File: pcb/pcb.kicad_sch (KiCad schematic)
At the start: 72 parts

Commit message: A  RP2040_Minimal.kicad_sym A  RP2040_minimal.pretty/8-USON-Handsolder.kicad_mod A  RP2040_minimal.pretty/8-USON.kicad_mod A  RP2040_minimal.pretty/C_0402_1005Metric.kicad_mod A  RP2040_minimal.pretty/C_0603_1608Metric.kicad_mod A  RP2040_minimal.pretty/C_0603_1608Metric_Pad1.08x0.95mm_HandSolder.kicad_mod A  RP2040_minimal.pretty/C_1206_3216Metric.kicad_mod A  RP2040_minimal.pretty/Crystal_SMD_2520-4Pin_2.5x2.0mm-Handsolder.kicad_mod A  RP2040_minimal.pretty/Crystal_SMD_HC49-US.kicad_mod A  RP2040_minimal.pretty/D_0402_1005Metric.kicad_mod A  RP2040_minimal.pretty/D_SOD-523.kicad_mod A  RP2040_minimal.pretty/Diodes_U_DFN1212_3.kicad_mod A  RP2040_minimal.pretty/Diodes_U_DFN1212_3_Handsolder.kicad_mod A  RP2040_minimal.pretty/LED_0402_1005Metric.kicad_mod A  RP2040_minimal.pretty/LED_Driver_Mod_Conn.kicad_mod A  RP2040_minimal.pretty/LED_Driver_Mod_Conn_1.27.kicad_mod A  RP2040_minimal.pretty/Module_Conn_Regular.kicad_mod A  RP2040_minimal.pretty/Module_Conn_Regular2.kicad_mod A  RP2040_minimal.pretty/Module_Conn_Regular_Outline.kicad_mod A  RP2040_minimal.pretty/QFN-28-1EP_4x4mm_P0.4mm_EP2.3x2.3mm-Handsolder.kicad_mod A  RP2040_minimal.pretty/QFN-28-1EP_4x4mm_P0.4mm_EP2.3x2.3mm.kicad_mod A  RP2040_minimal.pretty/RP2040-QFN-56-Handsolder.kicad_mod A  RP2040_minimal.pretty/RP2040-QFN-56.kicad_mod A  RP2040_minimal.pretty/R_0402_1005Metric.kicad_mod A  RP2040_minimal.pretty/R_0603_1608Metric_Pad0.98x0.95mm_HandSolder.kicad_mod A  RP2040_minimal.pretty/SW_CK_KXT3.kicad_mod A  RP2040_minimal.pretty/SW_SPST_Panasonic_EVPAF.kicad_mod A  RP2040_minimal.pretty/SW_Side_EVPAV.kicad_mod A  RP2040_minimal.pretty/SW_XKB_TS_2030.kicad_mod A  RP2040_minimal.pretty/USB_Micro-B_Amphenol_10103594-0001LF_Horizontal_modified.kicad_mod A  RP2040_minimal.pretty/XSON-8-1EP_4x4mm.kicad_mod M  border.py M  notes/notes.md M  pcb/fp-lib-table M  pcb/pcb.kicad_pcb M  pcb/pcb.kicad_prl M  pcb/pcb.kicad_sch M  plate/plate.kicad_pcb M  plate/plate.kicad_sch R  tmr-footprints/Switch_Cutout2_MX.kic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
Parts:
- S64, S66: footprint tmr-lib:sw_lowpro_combo_MDT -> tmr-lib:sw_lowpro_combo_2u_MDT
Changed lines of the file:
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@@
 			)
 		)
-		(property "Footprint" "tmr-lib:sw_lowpro_combo_MDT"
+		(property "Footprint" "tmr-lib:sw_lowpro_combo_2u_MDT"
 			(at 132.08 147.32 0)
 			(effects
@@
 			)
 		)
-		(property "Footprint" "tmr-lib:sw_lowpro_combo_MDT"
+		(property "Footprint" "tmr-lib:sw_lowpro_combo_2u_MDT"
 			(at 172.72 147.32 0)
 			(effects

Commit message: M  border.py A  notes/keyfrequency M  pcb/pcb.kicad_pcb M  pcb/pcb.kicad_prl M  pcb/pcb.kicad_sch M  place.py A  tmr-footprints/LED-6028.kicad_mod D  tmr-footprints/LED_1206_THT.kicad_mod M  tmr-footprints/sw_lowpro_combo_2u_MDT.kicad_mod A  tmr-footprints/sw_lowpro_combo_2u_MDT_L.kicad_mod A  tmr-footprints/sw_lowpro_combo_2u_MDT_R.kicad_mod M  tmr-footprints/sw_lowpro_combo_MDT.kicad_mod M  tmr-footprints/sw_lowpro_combo_MDT_led.kicad_mod
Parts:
- S64: footprint tmr-lib:sw_lowpro_combo_2u_MDT -> tmr-lib:sw_lowpro_combo_2u_MDT_L
- S66: footprint tmr-lib:sw_lowpro_combo_2u_MDT -> tmr-lib:sw_lowpro_combo_2u_MDT_R
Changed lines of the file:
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@@
 			)
 		)
-		(property "Footprint" "tmr-lib:sw_lowpro_combo_2u_MDT"
+		(property "Footprint" "tmr-lib:sw_lowpro_combo_2u_MDT_L"
 			(at 132.08 147.32 0)
 			(effects
@@
 			)
 		)
-		(property "Footprint" "tmr-lib:sw_lowpro_combo_2u_MDT"
+		(property "Footprint" "tmr-lib:sw_lowpro_combo_2u_MDT_R"
 			(at 172.72 147.32 0)
 			(effects

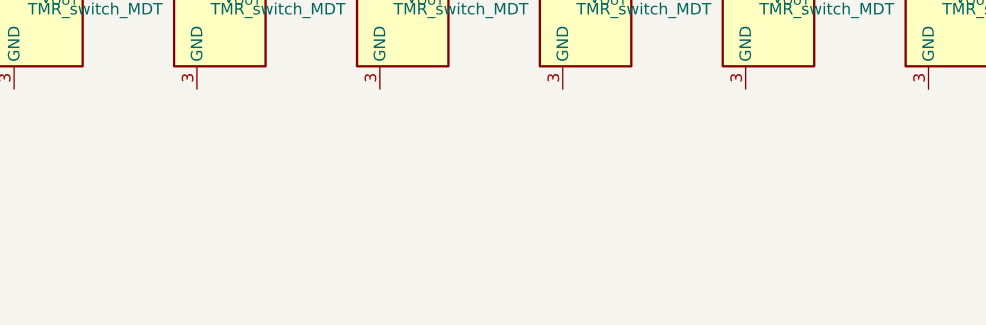
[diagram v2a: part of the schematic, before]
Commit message: M  notes/components.md M  pcb/pcb.kicad_pcb M  pcb/pcb.kicad_sch M  place.py D  tmr-footprints/sw_lowpro_combo_2u_MDT.kicad_mod D  tmr-footprints/sw_lowpro_combo_2u_MDT_L.kicad_mod D  tmr-footprints/sw_lowpro_combo_2u_MDT_R.kicad_mod M  tmr-footprints/sw_lowpro_combo_MDT.kicad_mod A  tmr-footprints/sw_lowpro_stab_2u.kicad_mod M  tmr-symbols.kicad_sym
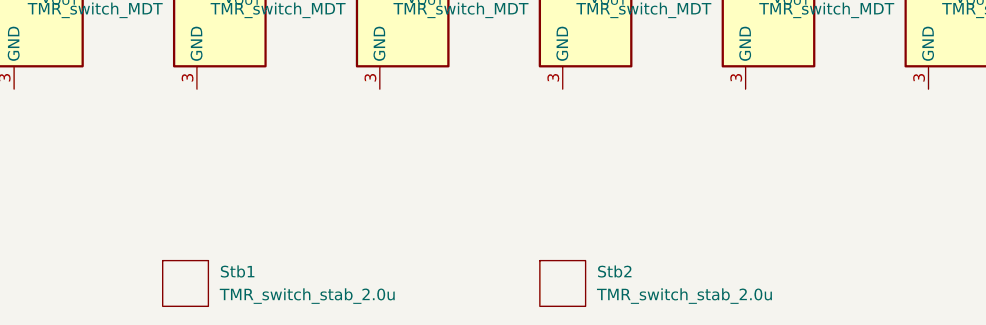
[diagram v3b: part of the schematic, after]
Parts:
- added Stb1, Stb2: TMR_switch_stab_2.0u, tmr-lib:sw_lowpro_stab_2u, symbol tmr-lib:TMR_switch_stab_2.0u
- S64: footprint tmr-lib:sw_lowpro_combo_2u_MDT_L -> tmr-lib:sw_lowpro_combo_MDT
- S66: footprint tmr-lib:sw_lowpro_combo_2u_MDT_R -> tmr-lib:sw_lowpro_combo_MDT
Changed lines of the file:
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@@
 			)
 		)
-		(property "Footprint" "tmr-lib:sw_lowpro_combo_2u_MDT_L"
+		(property "Footprint" "tmr-lib:sw_lowpro_combo_MDT"
 			(at 132.08 147.32 0)
 			(effects
@@
 	)
 	(symbol
+		(lib_id "tmr-lib:TMR_switch_stab_2.0u")
+		(at 46.99 179.07 0)
+		(unit 1)
+		(exclude_from_sim no)
+		(in_bom yes)
+		(on_board yes)
+		(dnp no)
+		(fields_autoplaced yes)
+		(property "Reference" "Stb1"
+			(at 50.8 177.7999 0)
+			(effects
+				(font
+					(size 1.27 1.27)
+				)
+				(justify left)
+			)
+		)
+		(property "Value" "TMR_switch_stab_2.0u"
+			(at 50.8 180.3399 0)
+			(effects
+				(font
+					(size 1.27 1.27)
+				)
+				(justify left)
+			)
+		)
+		(property "Footprint" "tmr-lib:sw_lowpro_stab_2u"
+			(at 46.99 179.07 0)
+			(effects
+				(font
+					(size 1.27 1.27)
+				)
+				(hide yes)
+			)
+		)
+		(property "Datasheet" ""
+			(at 46.99 179.07 0)
+			(effects
+				(font
+					(size 1.27 1.27)
+				)
+				(hide yes)
+			)
+		)
+		(property "Description" ""
+			(at 46.99 179.07 0)
+			(effects
+				(font
+					(size 1.27 1.27)
+				)
+				(hide yes)
+			)
+		)
+		(instances
+			(project ""
+				(path "/672ae9a0-2ac9-4023-9977-e9626ff99f32"
+					(reference "Stb1")
+					(unit 1)
+				)
+			)
+		)
+	)
+	(symbol
 		(lib_id "tmr-lib:TMR_switch_MDT")
 		(at 274.32 69.85 0)
@@
 	)
 	(symbol
+		(lib_id "tmr-lib:TMR_switch_stab_2.0u")
+		(at 88.9 179.07 0)
+		(unit 1)
+		(exclude_from_sim no)
+		(in_bom yes)
+		(on_board yes)
+		(dnp no)
+		(fields_autoplaced yes)
+		(property "Reference" "Stb2"
+			(at 92.71 177.7999 0)
+			(effects
+				(font
+					(size 1.27 1.27)
+				)
+				(justify left)
+			)
+		)
+		(property "Value" "TMR_switch_stab_2.0u"
+			(at 92.71 180.3399 0)
+			(effects
+				(font
+					(size 1.27 1.27)
+				)
+				(justify left)
+			)
+		)
+		(property "Footprint" "tmr-lib:sw_lowpro_stab_2u"
+			(at 88.9 179.07 0)
+			(effects
+				(font
+					(size 1.27 1.27)
+				)
+				(hide yes)
+			)
+		)
+		(property "Datasheet" ""
+			(at 88.9 179.07 0)
+			(effects
+				(font
+					(size 1.27 1.27)
+				)
+				(hide yes)
+			)
+		)
+		(property "Description" ""
+			(at 88.9 179.07 0)
+			(effects
+				(font
+					(size 1.27 1.27)
+				)
+				(hide yes)
+			)
+		)
+		(instances
+			(project ""
+				(path "/672ae9a0-2ac9-4023-9977-e9626ff99f32"
+					(reference "Stb2")
+					(unit 1)
+				)
+			)
+		)
+	)
+	(symbol
 		(lib_id "tmr-lib:TMR_switch_MDT")
 		(at 91.44 95.25 0)
@@
 			)
 		)
-		(property "Footprint" "tmr-lib:sw_lowpro_combo_2u_MDT_R"
+		(property "Footprint" "tmr-lib:sw_lowpro_combo_MDT"
 			(at 172.72 147.32 0)
 			(effects

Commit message: M  border.py M  notes/cnc.md M  notes/nRF52840.md M  notes/notes.md M  pcb/pcb.kicad_pcb M  pcb/pcb.kicad_sch M  pcb/sym-lib-table M  place.py M  plate/plate.kicad_pcb M  plate/plate.kicad_sch A  tmr-footprints/IS31FL3731-SSOP-28_5.3x10.2mm_P0.65mm.kicad_mod A  tmr-footprints/MCP3208-SOIC-16_3.9x9.9mm_P1.27mm.kicad_mod M  tmr-footprints/sw_lowpro_combo_MDT.kicad_mod D  tmr-footprints/sw_lowpro_combo_MDT_led.kicad_mod
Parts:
- added ADC1, ADC2, ADC3, ADC4, ADC5, ADC6, ADC7, ADC8, ADC9: MCP3208, tmr-lib:MCP3208-SOIC-16_3.9x9.9mm_P1.27mm, symbol Analog_ADC:MCP3208
- added C1: 2.2uF, RP2040_Minimal:C_0603_1608Metric_Pad1.08x0.95mm_HandSolder, symbol Device:C_Small
- added C2: 10uF, RP2040_Minimal:C_1206_3216Metric, symbol Device:C_Small
- added C3: 10uF, RP2040_Minimal:C_0603_1608Metric_Pad1.08x0.95mm_HandSolder, symbol Device:C_Small
- added C4, C5: 100nF, RP2040_Minimal:C_0603_1608Metric_Pad1.08x0.95mm_HandSolder, symbol Device:C_Small
- added D1, D10, D11, D12, D13, D14, D15, D16, D17, D18, D19, D2, D20, D21, D22, D23, D24, D25, D26, D27, D28, D29, D3, D30, D31, D32, D33, D34, D35, D36, D37, D38, D39, D4, D40, D41, D42, D43, D44, D45, D46, D47, D48, D49, D5, D50, D51, D52, D53, D54, D55, D56, D57, D58, D59, D6, D60, D61, D62, D63, D64, D65, D66, D67, D68, D69, D7, D70, D71, D72, D8, D9: LED, tmr-lib:LED-6028, symbol Device:LED
- added H1, H2, H3, H4, H5, H6, H7, H8: MountingHole, giri:SMTSO_M2, symbol Mechanical:MountingHole
- added Hs1, Hs10, Hs11, Hs12, Hs13, Hs14, Hs15, Hs16, Hs17, Hs18, Hs2, Hs3, Hs4, Hs5, Hs6, Hs7, Hs8, Hs9: ~, giri:SMTSO_M2, symbol giri:MountingHoleSMD
- added JLC1: JLC_Order_Num, giri:JLC_Order_Num, symbol giri:JLC_Order_Num
- added LedDr1: IS31FL3731-QF, tmr-lib:IS31FL3731-SSOP-28_5.3x10.2mm_P0.65mm, symbol Driver_LED:IS31FL3731-QF
- added R1, R2: 10k, RP2040_Minimal:R_0603_1608Metric_Pad0.98x0.95mm_HandSolder, symbol Device:R
- added R10, R11: 20k, RP2040_Minimal:R_0603_1608Metric_Pad0.98x0.95mm_HandSolder, symbol Device:R_Small
- added R3: 1k, RP2040_Minimal:R_0603_1608Metric_Pad0.98x0.95mm_HandSolder, symbol Device:R
- added R4, R5: 5.1k, RP2040_Minimal:R_0603_1608Metric_Pad0.98x0.95mm_HandSolder, symbol Device:R
- added R6, R7, R8: 4.7k, RP2040_Minimal:R_0603_1608Metric_Pad0.98x0.95mm_HandSolder, symbol Device:R_Small
- added R9: 100k, RP2040_Minimal:R_0603_1608Metric_Pad0.98x0.95mm_HandSolder, symbol Device:R_Small
- added SW1, SW2: SW_DIP_x01_XKB_TS_2030, giri:SW_B3U-3000P, symbol RP2040_Minimal:SW_DIP_x01_XKB_TS_2030
- added USBCon1: USB_TYPE_C_Receptacle_16P, Connector_USB:USB_C_Receptacle_XKB_U262-16XN-4BVC11, symbol RP2040_Minimal:USB_TYPE_C_Receptacle_16P
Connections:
- new net: R5.1, USBCon1.A5 (CC1)
- new net: R4.1, USBCon1.B5 (CC2)
- new net +3V3: R1.1, R2.1, R6.1, R7.1, R8.1
- new net +5V: C2.2, C3.1, C4.1, LedDr1.2 (VCC)
- new net AD: LedDr1.18 (AD), R11.1
- new net CA1: D1.1 (K), D16.2 (A), D2.1 (K), D3.1 (K), D30.2 (A), D4.1 (K), D45.2 (A), D5.1 (K), D6.1 (K), D7.1 (K), D8.1 (K), LedDr1.21 (CA1)
- new net CA2: D1.2 (A), D16.1 (K), D17.1 (K), D18.1 (K), D19.1 (K), D20.1 (K), D21.1 (K), D22.1 (K), D23.1 (K), D31.2 (A), D46.2 (A), LedDr1.22 (CA2)
- new net CA3: D17.2 (A), D2.2 (A), D30.1 (K), D31.1 (K), D32.1 (K), D33.1 (K), D34.1 (K), D35.1 (K), D36.1 (K), D37.1 (K), D47.2 (A), LedDr1.23 (CA3)
- new net CA4: D18.2 (A), D3.2 (A), D32.2 (A), D45.1 (K), D46.1 (K), D47.1 (K), D48.1 (K), D49.1 (K), D50.1 (K), D51.1 (K), D52.1 (K), LedDr1.24 (CA4)
- new net CA5: D19.2 (A), D33.2 (A), D4.2 (A), D48.2 (A), LedDr1.25 (CA5)
- new net CA6: D20.2 (A), D34.2 (A), D49.2 (A), D5.2 (A), LedDr1.26 (CA6)
- new net CA7: D21.2 (A), D35.2 (A), D50.2 (A), D6.2 (A), LedDr1.27 (CA7)
- new net CA8: D22.2 (A), D36.2 (A), D51.2 (A), D7.2 (A), LedDr1.28 (CA8)
- new net CA9: D23.2 (A), D37.2 (A), D52.2 (A), D8.2 (A), LedDr1.1 (CA9)
- new net CB1: D10.1 (K), D11.1 (K), D12.1 (K), D13.1 (K), D14.1 (K), D15.1 (K), D24.2 (A), D38.2 (A), D53.2 (A), D59.2 (A), D66.2 (A), D67.2 (A), D9.1 (K), LedDr1.7 (CB1)
- new net CB2: D24.1 (K), D25.1 (K), D26.1 (K), D27.1 (K), D28.1 (K), D29.1 (K), D39.2 (A), D54.2 (A), D60.2 (A), D65.2 (A), D68.2 (A), D9.2 (A), LedDr1.8 (CB2)
- new net CB3: D10.2 (A), D25.2 (A), D38.1 (K), D39.1 (K), D40.1 (K), D41.1 (K), D42.1 (K), D43.1 (K), D44.1 (K), D55.2 (A), D61.2 (A), D64.2 (A), D69.2 (A), LedDr1.9 (CB3)
- new net CB4: D11.2 (A), D26.2 (A), D40.2 (A), D53.1 (K), D54.1 (K), D55.1 (K), D56.1 (K), D57.1 (K), D58.1 (K), D62.2 (A), D63.2 (A), D70.2 (A), LedDr1.10 (CB4)
- new net CB5: D12.2 (A), D27.2 (A), D41.2 (A), D56.2 (A), D67.1 (K), D68.1 (K), D69.1 (K), D70.1 (K), D71.1 (K), D72.1 (K), LedDr1.11 (CB5)
- new net CB6: D13.2 (A), D28.2 (A), D42.2 (A), D57.2 (A), D63.1 (K), D64.1 (K), D65.1 (K), D66.1 (K), D71.2 (A), LedDr1.12 (CB6)
- new net CB7: D14.2 (A), D29.2 (A), D43.2 (A), D58.2 (A), D59.1 (K), D60.1 (K), D61.1 (K), D62.1 (K), D72.2 (A), LedDr1.13 (CB7)
- new net CB8: D15.2 (A), D44.2 (A), LedDr1.14 (CB8)
- new net C_FLT: C5.1, LedDr1.16 (C_FILT)
- new net GND: C1.1, C2.1, C3.2, C4.2, C5.2, LedDr1.29 (GND), LedDr1.5 (GND), R10.2, R11.2, R4.2, R5.2, R9.1, SW1.1, SW2.1, USBCon1.A1 (GND), USBCon1.A12 (GND), USBCon1.B1 (GND), USBCon1.B12 (GND), USBCon1.S1 (SHIELD)
- new net QSPI_SS: R2.2, R3.1
- new net RESET: R1.2, SW1.2
- new net R_EXT: LedDr1.6 (R_EXT), R10.1
- new net SCL: LedDr1.20 (SCL), R7.2
- new net SDA: LedDr1.19 (SDA), R6.2
- new net SDB: LedDr1.3 (~{SDB}), R9.2
- new net USB_D+: USBCon1.A6 (D1+), USBCon1.B6 (D2+)
- new net USB_D-: USBCon1.A7 (D1-), USBCon1.B7 (D2-)
- new net VBUS: C1.2, USBCon1.A4 (VBUS), USBCon1.A9 (VBUS), USBCon1.B4 (VBUS), USBCon1.B9 (VBUS)
- new net ~{INTB}: LedDr1.4 (~{INTB}), R8.2
- new net ~{USB_BOOT}: R3.2, SW2.2
- no-connect marks 0 -> 4
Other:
- note added: "BOM:"
- note added: "Boot"
- note added: "Filter / VCC Cap"
- note added: "Holes"
- note added: "LED Driver"
- note added: "LEDs"
- note added: "Power"
- note added: "Pull up / down"
- note added: "Reset"
- note added: "Switches"
- note added: "Tactile switch: Alps: SKSF, SKSGACE010, side SKSCPBE010 Panasonic: EVPAL7A1AB24, EVPAF7B70, side mount EVPAVAA1A, EVPAEGE2A, EVPAEBB2A Omron: B3U-1000P, side B3U-3000P"
- note added: "USB TYPE C"
- note removed: "Switch Matrix"
- moved on the sheet: Stb1, Stb2

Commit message: M  border.py M  notes/notes.md M  pcb/pcb.kicad_pcb M  pcb/pcb.kicad_prl M  pcb/pcb.kicad_pro M  pcb/pcb.kicad_sch M  pcb/sym-lib-table M  place.py M  tmr-footprints/C_0603_1608Metric.kicad_mod D  tmr-footprints/C_0805_2012Metric.kicad_mod A  tmr-footprints/C_1206_3216Metric.kicad_mod A  tmr-footprints/IS31FL3731-RECESSED-SSOP-28_5.3x10.2mm_P0.65mm.kicad_mod M  tmr-footprints/JLC_Order_Num.kicad_mod M  tmr-footprints/LED-6028.kicad_mod A  tmr-footprints/MCP3208-RECESSED-SOIC-16_3.9x9.9mm_P1.27mm.kicad_mod M  tmr-footprints/MCP3208-SOIC-16_3.9x9.9mm_P1.27mm.kicad_mod A  tmr-footprints/MountingHole_5.3mm_M5_ISO14580_Pad_TopBottom.kicad_mod A  tmr-footprints/R_0603_1608Metric.kicad_mod A  tmr-footprints/SMTSO_M1.6.kicad_mod A  tmr-footprints/SW_B3U-3000P.kicad_mod A  tmr-footprints/sw_lowpro_gateron_MDT.kicad_mod M  tmr-symbols.kicad_sym
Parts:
- removed ADC5: MCP3208, tmr-lib:MCP3208-SOIC-16_3.9x9.9mm_P1.27mm, symbol Analog_ADC:MCP3208
- removed Hs11, Hs12, Hs13, Hs14, Hs15, Hs16, Hs17, Hs18: ~, giri:SMTSO_M2, symbol giri:MountingHoleSMD
- added ADC3: MCP3208, tmr-lib:MCP3208-SOIC-16_3.9x9.9mm_P1.27mm, symbol Analog_ADC:MCP3208
- added C1, C2, C3, C4, C5, C6, C7, C8, C9: C_Small_US, tmr-lib:C_0603_1608Metric, symbol Device:C_Small_US
- added C10, C11, C12, C13, C14, C15, C16, C17, C18, C22: 100nF, tmr-lib:C_0603_1608Metric, symbol Device:C_Small
- added C20, C21, C26: 1uF, tmr-lib:C_0603_1608Metric, symbol Device:C_Small
- added C23, C25: 2.2uF, tmr-lib:C_0603_1608Metric, symbol Device:C_Small
- added C24: 10uF, tmr-lib:C_0603_1608Metric, symbol Device:C_Small
- added C31, C32: 15pF, tmr-lib:C_0603_1608Metric, symbol Device:C_Small
- added R14: 1k, tmr-lib:R_0603_1608Metric, symbol Device:R
- added R4, R5: 27R, tmr-lib:R_0603_1608Metric, symbol Device:R
- added U1: RP2040, rp2040:RP2040-QFN-56, symbol RP2040_Minimal:RP2040
- added U2: Memory_Flash_W25Q64_XSON, rp2040:8-USON, symbol RP2040_Minimal:Memory_Flash_W25Q64_XSON
- added U3: NCP114ASN330T1G, Package_SO:TSOP-5_1.65x3.05mm_P0.95mm, symbol RP2040_Minimal:Regulator_LDO_ONS_NCP114_TSOP5
- added X1: 12.000MHz, rp2040:Crystal_SMD_2520-4Pin_2.5x2.0mm-Handsolder, symbol RP2040_Minimal:Crystal_P4
- C19: renamed from C1; footprint RP2040_Minimal:C_0603_1608Metric_Pad1.08x0.95mm_HandSolder -> tmr-lib:C_0603_1608Metric
- C27: renamed from C2; footprint RP2040_Minimal:C_1206_3216Metric -> tmr-lib:C_1206_3216Metric
- C28: renamed from C3; footprint RP2040_Minimal:C_0603_1608Metric_Pad1.08x0.95mm_HandSolder -> tmr-lib:C_0603_1608Metric
- C29: renamed from C4; footprint RP2040_Minimal:C_0603_1608Metric_Pad1.08x0.95mm_HandSolder -> tmr-lib:C_0603_1608Metric
- C30: renamed from C5; footprint RP2040_Minimal:C_0603_1608Metric_Pad1.08x0.95mm_HandSolder -> tmr-lib:C_0603_1608Metric
- H1, H2, H3, H4, H5, H6, H7, H8: footprint giri:SMTSO_M2 -> tmr-lib:MountingHole_5.3mm_M5_ISO14580_Pad_TopBottom
- Hs1, Hs10, Hs2, Hs3, Hs4, Hs5, Hs6, Hs7, Hs8, Hs9: footprint giri:SMTSO_M2 -> tmr-lib:SMTSO_M1.6
- JLC1: footprint giri:JLC_Order_Num -> tmr-lib:JLC_Order_Num
- LedDr1: footprint tmr-lib:IS31FL3731-SSOP-28_5.3x10.2mm_P0.65mm -> rp2040:QFN-28-1EP_4x4mm_P0.4mm_EP2.3x2.3mm
- R1, R2, R3: footprint RP2040_Minimal:R_0603_1608Metric_Pad0.98x0.95mm_HandSolder -> tmr-lib:R_0603_1608Metric
- R10: renamed from R8; footprint RP2040_Minimal:R_0603_1608Metric_Pad0.98x0.95mm_HandSolder -> tmr-lib:R_0603_1608Metric
- R11: renamed from R9; footprint RP2040_Minimal:R_0603_1608Metric_Pad0.98x0.95mm_HandSolder -> tmr-lib:R_0603_1608Metric
- R12: renamed from R10; footprint RP2040_Minimal:R_0603_1608Metric_Pad0.98x0.95mm_HandSolder -> tmr-lib:R_0603_1608Metric
- R13: renamed from R11; footprint RP2040_Minimal:R_0603_1608Metric_Pad0.98x0.95mm_HandSolder -> tmr-lib:R_0603_1608Metric
- R6: renamed from R4; footprint RP2040_Minimal:R_0603_1608Metric_Pad0.98x0.95mm_HandSolder -> tmr-lib:R_0603_1608Metric
- R7: renamed from R5; footprint RP2040_Minimal:R_0603_1608Metric_Pad0.98x0.95mm_HandSolder -> tmr-lib:R_0603_1608Metric
- R8: renamed from R6; footprint RP2040_Minimal:R_0603_1608Metric_Pad0.98x0.95mm_HandSolder -> tmr-lib:R_0603_1608Metric
- R9: renamed from R7; footprint RP2040_Minimal:R_0603_1608Metric_Pad0.98x0.95mm_HandSolder -> tmr-lib:R_0603_1608Metric
- S1, S10, S11, S12, S13, S14, S15, S16, S17, S18, S19, S2, S20, S21, S22, S23, S24, S25, S26, S27, S28, S29, S3, S30, S31, S32, S33, S34, S35, S36, S37, S38, S39, S4, S40, S41, S42, S43, S44, S45, S46, S47, S48, S49, S5, S50, S51, S52, S53, S54, S55, S56, S57, S58, S59, S6, S60, S61, S62, S63, S64, S65, S66, S67, S68, S69, S7, S70, S71, S72, S8, S9: footprint tmr-lib:sw_lowpro_combo_MDT -> tmr-lib:sw_lowpro_gateron_MDT
- SW1, SW2: footprint giri:SW_B3U-3000P -> Button_Switch_SMD:SW_SPST_B3U-3000P
- renumbered ADC3 to ADC5
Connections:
- net +3V3: now also ADC1.15 (Vref), ADC1.16 (Vdd), ADC2.15 (Vref), ADC2.16 (Vdd), ADC4.15 (Vref), ADC4.16 (Vdd), ADC5.15 (Vref), ADC5.16 (Vdd), ADC6.15 (Vref), ADC6.16 (Vdd), ADC7.15 (Vref), ADC7.16 (Vdd), ADC8.15 (Vref), ADC8.16 (Vdd), ADC9.15 (Vref), ADC9.16 (Vdd), S1.1 (V_{CC}), S10.1 (V_{CC}), S11.1 (V_{CC}), S12.1 (V_{CC}), S13.1 (V_{CC}), S14.1 (V_{CC}), S15.1 (V_{CC}), S16.1 (V_{CC}), S17.1 (V_{CC}), S18.1 (V_{CC}), S19.1 (V_{CC}), S2.1 (V_{CC}), S20.1 (V_{CC}), S21.1 (V_{CC}), S22.1 (V_{CC}), S23.1 (V_{CC}), S24.1 (V_{CC}), S25.1 (V_{CC}), S26.1 (V_{CC}), S27.1 (V_{CC}), S28.1 (V_{CC}), S29.1 (V_{CC}), S3.1 (V_{CC}), S30.1 (V_{CC}), S31.1 (V_{CC}), S32.1 (V_{CC}), S33.1 (V_{CC}), S34.1 (V_{CC}), S35.1 (V_{CC}), S36.1 (V_{CC}), S37.1 (V_{CC}), S38.1 (V_{CC}), S39.1 (V_{CC}), S4.1 (V_{CC}), S40.1 (V_{CC}), S41.1 (V_{CC}), S42.1 (V_{CC}), S43.1 (V_{CC}), S44.1 (V_{CC}), S45.1 (V_{CC}), S46.1 (V_{CC}), S47.1 (V_{CC}), S48.1 (V_{CC}), S49.1 (V_{CC}), S5.1 (V_{CC}), S50.1 (V_{CC}), S51.1 (V_{CC}), S52.1 (V_{CC}), S53.1 (V_{CC}), S54.1 (V_{CC}), S55.1 (V_{CC}), S56.1 (V_{CC}), S57.1 (V_{CC}), S58.1 (V_{CC}), S59.1 (V_{CC}), S6.1 (V_{CC}), S60.1 (V_{CC}), S61.1 (V_{CC}), S62.1 (V_{CC}), S63.1 (V_{CC}), S64.1 (V_{CC}), S65.1 (V_{CC}), S66.1 (V_{CC}), S67.1 (V_{CC}), S68.1 (V_{CC}), S69.1 (V_{CC}), S7.1 (V_{CC}), S70.1 (V_{CC}), S71.1 (V_{CC}), S72.1 (V_{CC}), S8.1 (V_{CC}), S9.1 (V_{CC}), ADC3.15 (Vref), ADC3.16 (Vdd), C1.1, C12.1, C13.1, C14.1, C15.1, C16.1, C17.1, C18.1, C2.1, C21.1, C22.1, C23.1, C24.1, C26.1, C3.1, C4.1, C5.1, C6.1, C7.1, C8.1, C9.1, U1.1 (IOVDD), U1.10 (IOVDD), U1.22 (IOVDD), U1.33 (IOVDD), U1.42 (IOVDD), U1.43 (ADC_AVDD), U1.44 (VREG_IN), U1.48 (USB_VDD), U1.49 (IOVDD), U2.8 (VCC), U3.5 (VOUT)
- net GND: now also ADC1.14 (AGND), ADC1.9 (DGND), ADC2.14 (AGND), ADC2.9 (DGND), ADC4.14 (AGND), ADC4.9 (DGND), ADC5.14 (AGND), ADC5.9 (DGND), ADC6.14 (AGND), ADC6.9 (DGND), ADC7.14 (AGND), ADC7.9 (DGND), ADC8.14 (AGND), ADC8.9 (DGND), ADC9.14 (AGND), ADC9.9 (DGND), S1.3 (GND), S10.3 (GND), S11.3 (GND), S12.3 (GND), S13.3 (GND), S14.3 (GND), S15.3 (GND), S16.3 (GND), S17.3 (GND), S18.3 (GND), S19.3 (GND), S2.3 (GND), S20.3 (GND), S21.3 (GND), S22.3 (GND), S23.3 (GND), S24.3 (GND), S25.3 (GND), S26.3 (GND), S27.3 (GND), S28.3 (GND), S29.3 (GND), S3.3 (GND), S30.3 (GND), S31.3 (GND), S32.3 (GND), S33.3 (GND), S34.3 (GND), S35.3 (GND), S36.3 (GND), S37.3 (GND), S38.3 (GND), S39.3 (GND), S4.3 (GND), S40.3 (GND), S41.3 (GND), S42.3 (GND), S43.3 (GND), S44.3 (GND), S45.3 (GND), S46.3 (GND), S47.3 (GND), S48.3 (GND), S49.3 (GND), S5.3 (GND), S50.3 (GND), S51.3 (GND), S52.3 (GND), S53.3 (GND), S54.3 (GND), S55.3 (GND), S56.3 (GND), S57.3 (GND), S58.3 (GND), S59.3 (GND), S6.3 (GND), S60.3 (GND), S61.3 (GND), S62.3 (GND), S63.3 (GND), S64.3 (GND), S65.3 (GND), S66.3 (GND), S67.3 (GND), S68.3 (GND), S69.3 (GND), S7.3 (GND), S70.3 (GND), S71.3 (GND), S72.3 (GND), S8.3 (GND), S9.3 (GND), ADC3.14 (AGND), ADC3.9 (DGND), C1.2, C10.2, C11.2, C12.2, C13.2, C14.2, C15.2, C16.2, C17.2, C18.2, C2.2, C20.2, C21.2, C22.2, C23.2, C24.2, C25.2, C26.2, C3.2, C31.2, C32.2, C4.2, C5.2, C6.2, C7.2, C8.2, C9.2, U1.19 (TESTEN), U1.57 (GND), U2.4 (GND), U2.9 (EP), U3.2 (GND), X1.2, X1.4
- net QSPI_SS: now also U1.56 (QSPI_SS), U2.1 (~{CS)
- net USB_D+: now also R4.2
- net USB_D-: now also R5.2
- net VBUS: now also C25.1, U3.1 (IN), U3.3 (EN)
- new net: C31.1, R14.2, X1.1
- new net +1V1: C10.1, C11.1, C20.1, U1.23 (DVDD), U1.45 (VREG_VOUT), U1.50 (DVDD)
- new net D+: R4.1, U1.47 (USB_DP)
- new net D-: R5.1, U1.46 (USB_DM)
- new net GPIO0: U1.2 (GPIO0)
- new net GPIO1: U1.3 (GPIO1)
- new net GPIO10: U1.13 (GPIO10)
- new net GPIO11: U1.14 (GPIO11)
- new net GPIO12: U1.15 (GPIO12)
- new net GPIO13: U1.16 (GPIO13)
- new net GPIO14: U1.17 (GPIO14)
- new net GPIO15: U1.18 (GPIO15)
- new net GPIO16: U1.27 (GPIO16)
- new net GPIO17: U1.28 (GPIO17)
- new net GPIO18: U1.29 (GPIO18)
- new net GPIO19: U1.30 (GPIO19)
- new net GPIO2: U1.4 (GPIO2)
- new net GPIO20: U1.31 (GPIO20)
- new net GPIO21: U1.32 (GPIO21)
- new net GPIO22: U1.34 (GPIO22)
- new net GPIO23: U1.35 (GPIO23)
- new net GPIO24: U1.36 (GPIO24)
- new net GPIO25: U1.37 (GPIO25)
- new net GPIO26: U1.38 (GPIO26_ADC0)
- new net GPIO27: U1.39 (GPIO27_ADC1)
- new net GPIO28: U1.40 (GPIO28_ADC2)
- new net GPIO29: U1.41 (GPIO29_ADC3)
- new net GPIO3: U1.5 (GPIO3)
- new net GPIO4: U1.6 (GPIO4)
- new net GPIO5: U1.7 (GPIO5)
- new net GPIO6: U1.8 (GPIO6)
- new net GPIO7: U1.9 (GPIO7)
- new net GPIO8: U1.11 (GPIO8)
- new net GPIO9: U1.12 (GPIO9)
- new net QSPI_SCLK: U1.52 (QSPI_SCLK), U2.6 (CLK)
- new net QSPI_SD0: U1.53 (QSPI_SD0), U2.5 (DI_(IO0))
- new net QSPI_SD1: U1.55 (QSPI_SD1), U2.2 (DO_(IO1))
- new net QSPI_SD2: U1.54 (QSPI_SD2), U2.3 (~{WP}_(IO2))
- new net QSPI_SD3: U1.51 (QSPI_SD3), U2.7 (~{HOLD}_(IO3))
- new net RUN: U1.26 (RUN)
- new net SWCLK: U1.24 (SWCLK)
- new net SWD: U1.25 (SWD)
- new net XIN: C32.1, U1.20 (XIN), X1.3
- new net XOUT: R14.1, U1.21 (XOUT)
- no-connect marks 4 -> 5
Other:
- note added: "3.3V/300mA LDO"
- note added: "4-64Mbit Flash, Quad SPI, 100-133MHz, XIP (eXecute In Place), 3.3V: USON 2x3x.6 mm Winbond: W25Q16JVUXIQ (2MB, 133 MHz) GigaDevice: GD25Q40CEIGR (512kB, 120MHz) GigaDevice: GD25Q80CEIGR (1MB, 120 MHz) GigaDevice: GD25Q80EEIGR (1MB, 133MHz) ISSI: IS25LP080D-JULE (1MB, 133 MHz) WSON-8 5x6mm: Winbond W25Q128JV 16MB C190862 XSON-8 4x4mm: Winbond W25Q64JV 8MB C2940195"
- note added: "Crystal"
- note added: "Crystal 12MHz, 2520 SMD package: JYJE: 2TJ412000NYGBC JGHC: S22120001210120 Yangxing Tech: X252012MMB4SI-24 Seiko Epson: Q24FA20H0068700 ECS: ECS-120-12-36-AGN-TR3"
- note added: "LDO"
- note added: "LDO 3.3V/300mA, TSOP5 package: On Semi NCP114ASN330T1G Richtek RT9078-33GJ5"
- note added: "Make sure these two R's are close to RP2040"
- note added: "Make sure this C is close to pin 44 of RP2040"
- note added: "Make sure this C is close to pin 45 of RP2040"
- note added: "NCP114: Input Capacitor Selection (CIN) It is recommended to connect at least a 1uF Ceramic X5R or X7R capacitor as close as possible to the IN pin of the device. Output Decoupling (COUT) The NCP114 requires an output capacitor connected as close as possible to the output pin of the regulator. The recommended capacitor value is 1uF and X7R or X5R dielectric due to its low capacitance variations o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"
- note added: "QSPI Flash"
- note added: "RP2040"
- moved on the sheet: ADC5, C19, H1, H2, H3, H4, H5, H6, H7, H8, Hs1, Hs10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
